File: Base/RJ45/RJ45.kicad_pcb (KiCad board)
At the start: 2 copper layers, 30 x 84 mm, 31 parts, among them J1 Barrel_Jack_Switch, J2 AudioJack2_Ground, J3 AudioJack2_Ground, J4 RJ45, U2 OPA1656

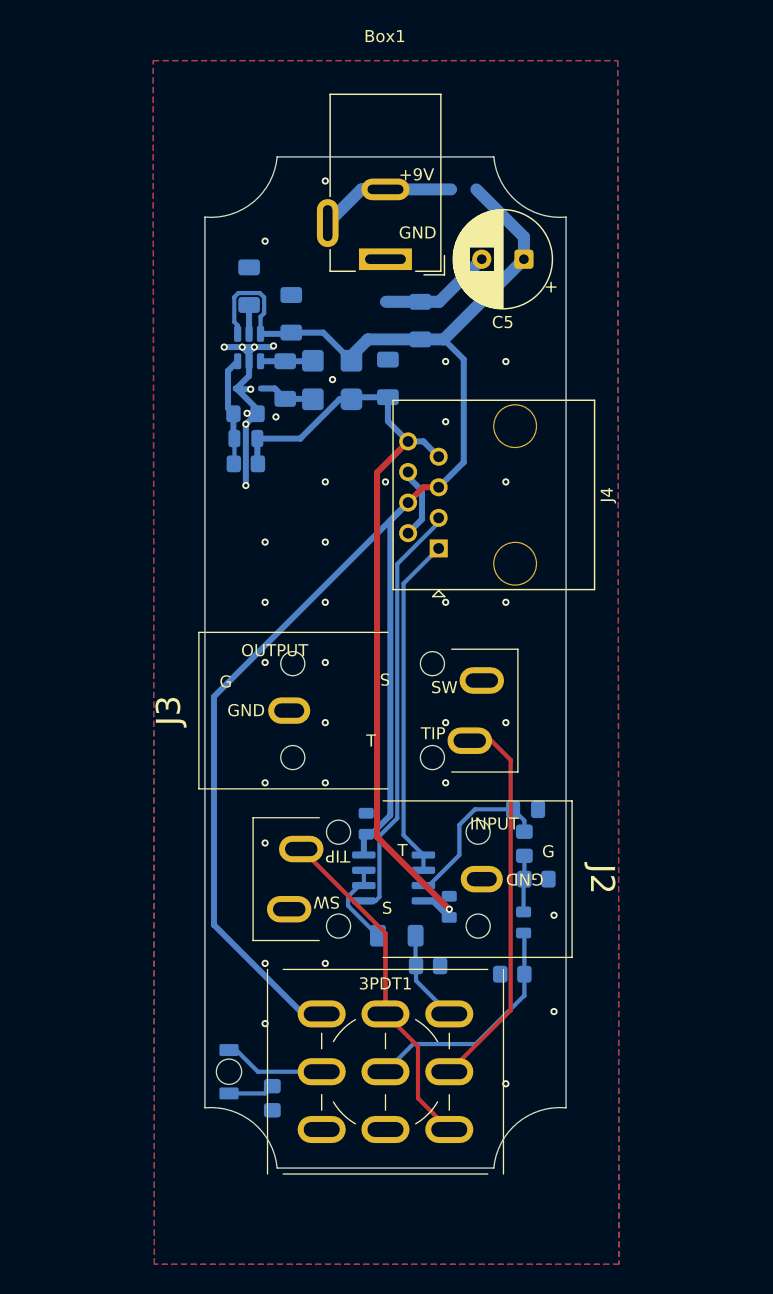
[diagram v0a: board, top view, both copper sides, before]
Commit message: Switch to a shielded RJ45 connector for the RJ45 test boards
It turns out that all my ethernet cables I had around look to be plain
unshielded twisted pairs (UTP), and some very preliminary testing shows
that they are very noisy and I'd need to use differential signalling to
make the whole "connect the base and effect with an ethernet cable"
scheme work.

I know, I know, that's technically the right thing to do anyway, but I
really don't think it's an option.  It adds way too much effort at the
effects end, at that point I'm better off just keeping the two together.

Even if some of my recent circuits have been differential (ie that whole
multiplier thing), I don't want to force that on everything.

And yes, the ethernet cable idea might have been a stupid idea and any
first-year EE would probably have told me that.  I'm a SW guy, remember?

But before giving up, let's just try the single-ended model with proper
shielded cables and shielded connectors.  The double-shielded cables are
a thing, with each twisted pair foil-shielded and then the whole cable
having a braided shield.

That would seem to be no worse than a normal 1/4" audio cable, even if
the same cable also carries power.  I'm looking for a few feet, not long
runs.  Knock wood.

And the shielding is part of the CAT8 specs, so this is standard cable
these days and cheap, even if my random box of cables was full of the
old crappy stuff of yesteryear.

So maybe this model is still salvageable with single-ended signaling.
Because I'd love to separate the stomp switch and audio jacks from the
actual effect side.

Signed-off-by: Linus Torvalds <torvalds@linux-foundation.org>
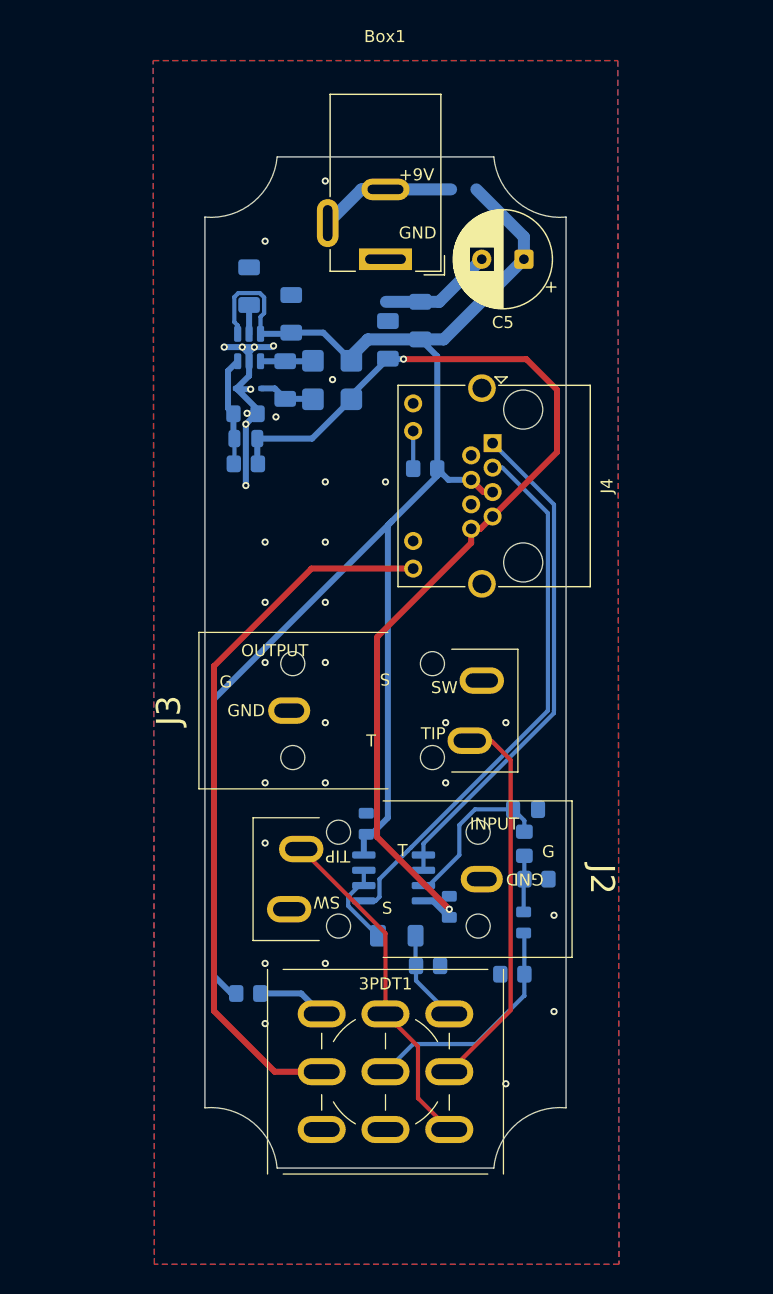
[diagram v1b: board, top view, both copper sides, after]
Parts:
- removed D3: LED, Mylib:Würth Reverse Mount LED
- added R1: 2.2k, Resistor_SMD:R_0805_2012Metric_Pad1.20x1.40mm_HandSolder, B.Cu at (103.3, 83.9)
- J4: value RJ45 -> RJ45_LED_Shielded; footprint Connector_RJ:RJ45_OST_PJ012-8P8CX_Vertical -> Connector_RJ:RJ45_Amphenol_RJHSE538X
- moved J4 9.83 mm to (108.9, 81.8), turned to -90 degrees
- moved R4 8.93 mm to (88.6, 127.5), turned to 0 degrees
- moved C4 3.20 mm to (100.2, 73.2)
- renumbered R1 to R2, R2 to R3, R3 to R4, R4 to R5, R5 to R6, R6 to R7, R7 to R8
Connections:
- 3PDT1 pad 1: +V -> Net-(3PDT1A-A1)
- 3PDT1 pad 2: Net-(3PDT1A-A2) -> LED^{ACTIVE}
- R4 pad 1: Net-(D3-K) -> +V
- R4 pad 2: GND -> Net-(3PDT1A-A1)
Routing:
- net LED^{ACTIVE}: track 0.00 -> 59.6 mm
- net -V: track 67.4 -> 86.7 mm, vias 1 -> 2
- net IN^{EFF}: track 28.6 -> 42.1 mm
- net OUT^{EFF}: track 34.6 -> 45.3 mm
- net Net-(3PDT1A-A2): track 7.85 -> 0.00 mm
- net Net-(3PDT1A-A1): track 0.00 -> 5.80 mm
- net GND: track 35.5 -> 29.9 mm, vias 39 -> 33
- net Net-(D3-K): track 3.85 -> 0.00 mm
- net +V: track 144.5 -> 140.7 mm
- net LED^{POWER}: track 0.00 -> 3.13 mm
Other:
- board text removed: "REF OUT IN +LED"

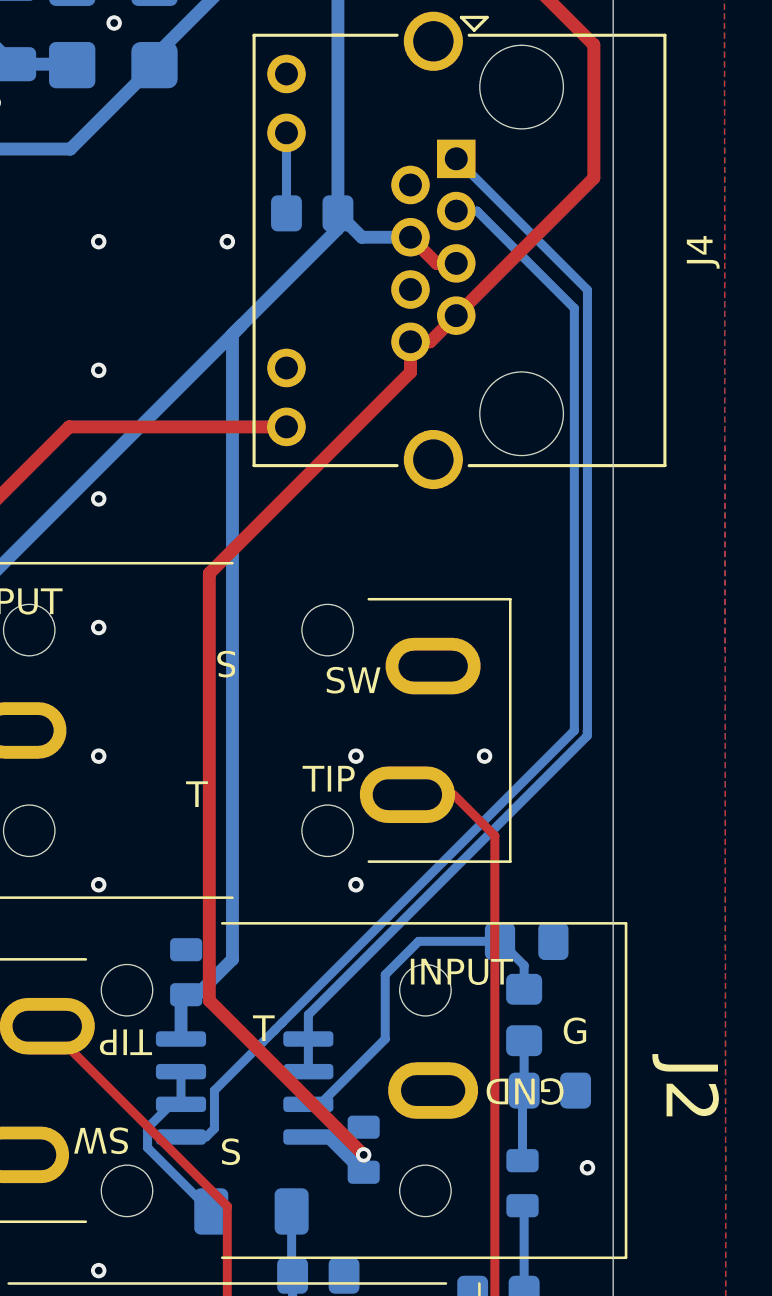
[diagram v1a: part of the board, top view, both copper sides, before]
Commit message: RJ45: hopefully make the base board actually work
Ok, with some boards back and populated, that whole "feed signal over
RJ45" didn't work at all.  I still think the concept should work, but my
implementation of it is obviously very broken.

The op amp output to the effect ends up oscillating wildly at a
frequency of a few MHz.  And while I might have screwed something else
up, I think it's because of a capacitive load in the form of that cable.

According to random searches I did, the minimal fix is typically to add
a small resistive load in series on the output.  So I did that.

But thinking about it, the other end is very possibly going to have the
same problem, and none of the existing effects boards were designed with
any of this in mind.

So I will also be updating the test board at the other end of the cable
to do active buffering and I suspect I really should rebias the signal
too at that point so that the existing effects boards see the
traditional VGND setup instead of the quick hack that just passively
changed the rules under them.

It may obviously still be the case that this is all just misguided
garbage, but before throwing it in the bin, let's try to do it right.
That includes adding some transmission line simulation, even if that
didn't actually show the issue (with or without the series resistor).

Maybe it's something else entirely that I'm not seeing / understanding.

Signed-off-by: Linus Torvalds <torvalds@linux-foundation.org>
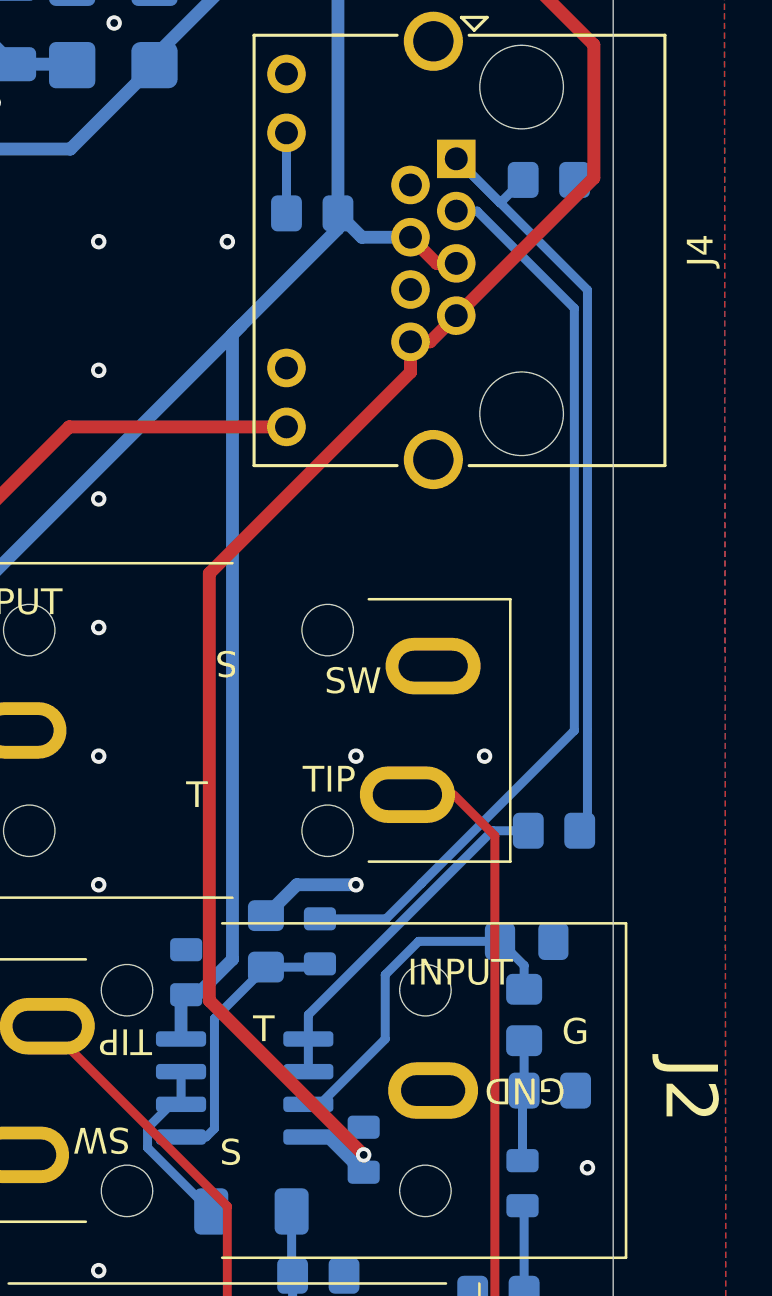
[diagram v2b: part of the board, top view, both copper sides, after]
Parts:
- added C12: 0.1uF, Mylib:C_0704_1810Metric, B.Cu at (103.6, 112.2)
- added R10: 100k, Resistor_SMD:R_0805_2012Metric_Pad1.20x1.40mm_HandSolder, B.Cu at (101.5, 112.2)
- added R6: 100R, Resistor_SMD:R_0805_2012Metric_Pad1.20x1.40mm_HandSolder, B.Cu at (112.7, 107.9)
- added R9: 100k, Resistor_SMD:R_0805_2012Metric_Pad1.20x1.40mm_HandSolder, B.Cu at (112.5, 82.6)
- renumbered C12 to C13, R8 to R11, R6 to R7, R7 to R8
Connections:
- U2 pad 1: IN^{EFF} -> Net-(U2A--)
- U2 pad 2: IN^{EFF} -> Net-(U2A--)
- U2 pad 5: OUT^{EFF} -> Net-(U2B-+)
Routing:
- net Net-(U2A--): track 0.00 -> 13.7 mm
- net Net-(U2B-+): track 0.00 -> 10.7 mm
- net IN^{EFF}: track 42.1 -> 32.0 mm
- net OUT^{EFF}: track 45.3 -> 35.5 mm
- net GND: track 29.9 -> 33.9 mm

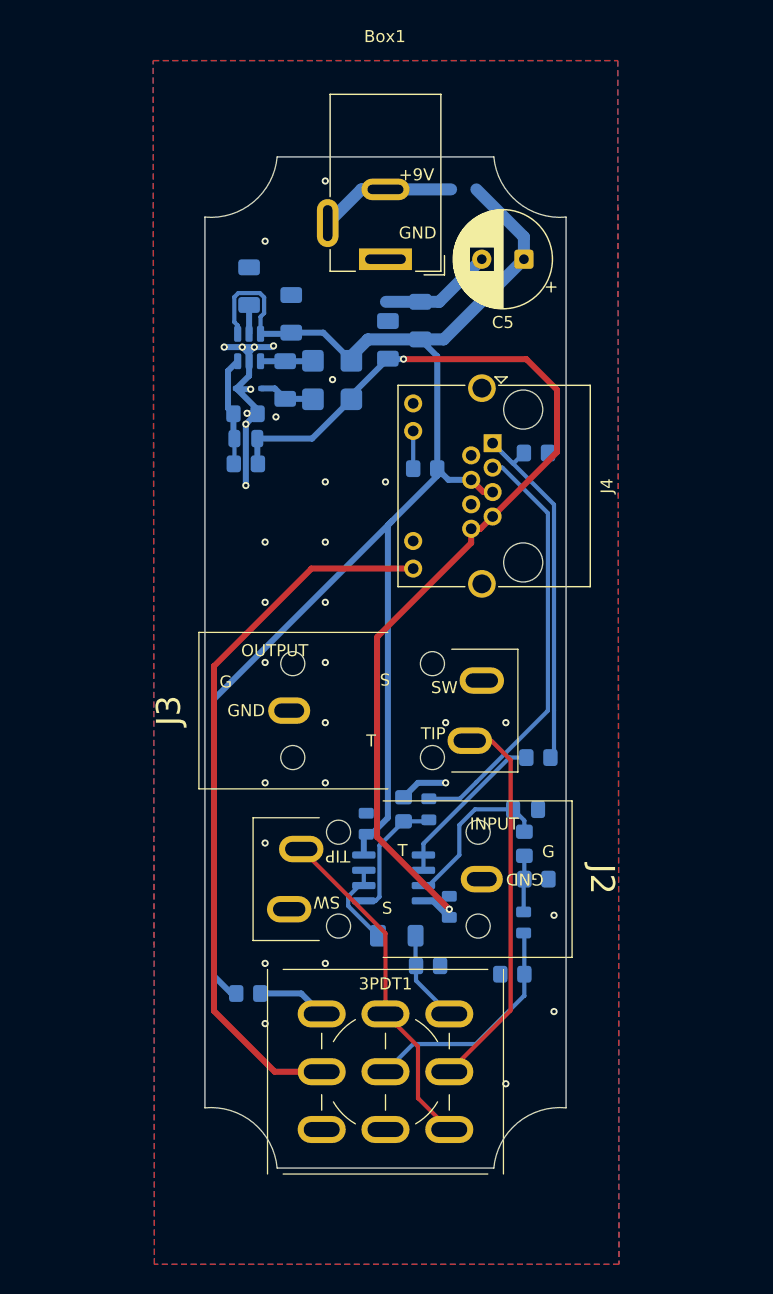
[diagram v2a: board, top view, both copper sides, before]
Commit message: Update the RJ45 boards
So I'm doing two different cable versions in parallel to see which I
like better.  The "passive base board" version uses USB-C connectors and
really doesn't do anything at all but convert the power, stomp switch
and audio connectors to one single cable.  So the effects board is
supposed to do everything that is actually signal-related, including
generating its own reference voltages etc.

In contrast, the RJ45 board is "active", and also generates a negative
power rail.  That doesn't help the existing effects boards, but it means
that any boards actively designed for this have all the voltages
(assuming +-9V and GND works for them), and don't need to rebias signals
etc.

Do I know which board - if any - I'm actually going to develop further?
No.  They may both be garbage.

Signed-off-by: Linus Torvalds <torvalds@linux-foundation.org>
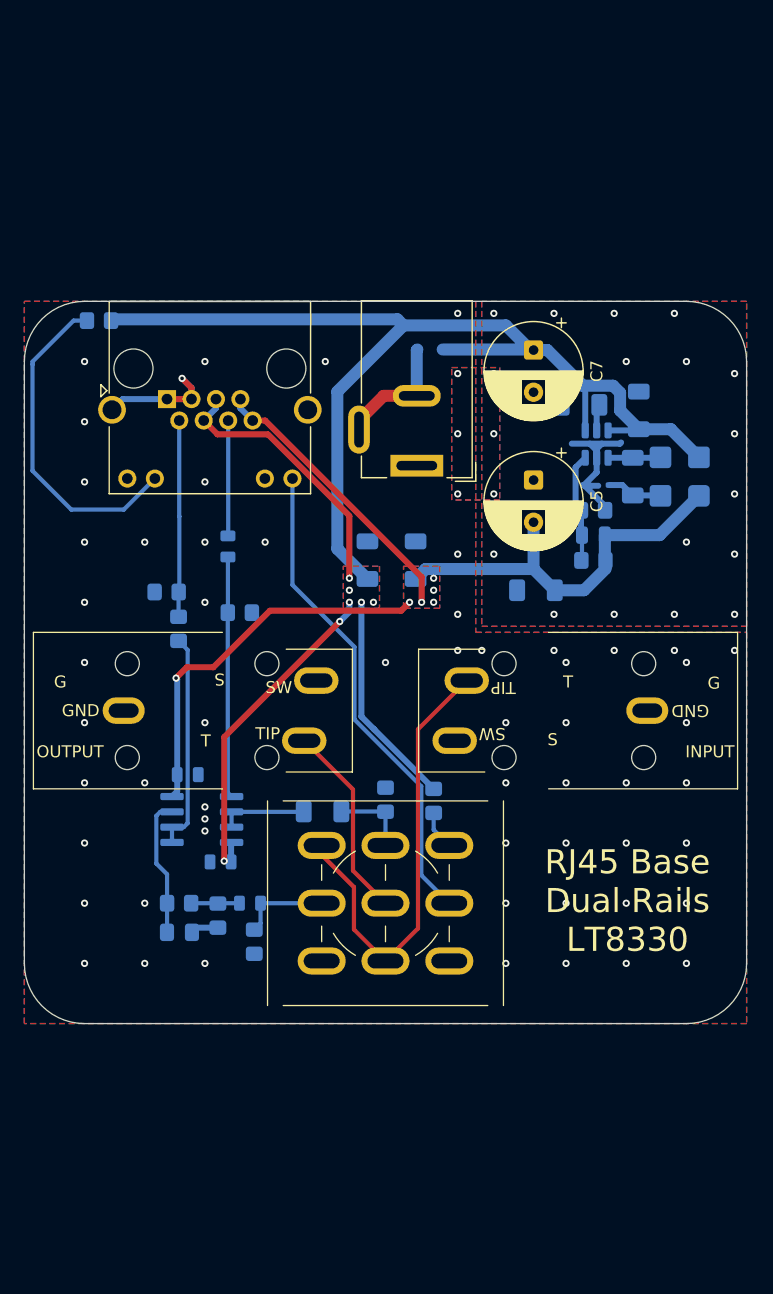
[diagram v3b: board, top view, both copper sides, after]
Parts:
- removed Box1: 1590A, Mylib:1590A
- added C5: 100uF, Capacitor_THT:CP_Radial_D8.0mm_P3.50mm, F.Cu at (112.3, 84.8)
- added C6: 10uF, Capacitor_SMD:C_1206_3216Metric_Pad1.33x1.80mm_HandSolder, B.Cu at (102.5, 91.5)
- moved R9 32.8 mm to (81.8, 94.1), turned to 180 degrees
- moved R6 31.7 mm to (82.8, 97.2), turned to 90 degrees
- moved C13 30.5 mm to (82.9, 122.4)
- moved C1 30.0 mm to (120.5, 84.6)
- moved C2 30.0 mm to (117.3, 89.4)
- moved C3 30.0 mm to (121.0, 79.1)
- moved D1 30.0 mm to (117.5, 85.3)
- moved L1 30.0 mm to (124.4, 84.6)
- moved R2 30.0 mm to (117.3, 91.5)
- moved R3 30.0 mm to (117.2, 87.4)
- moved U1 30.0 mm to (117.5, 81.9)
- moved R1 29.8 mm to (76.2, 71.6)
- moved C9 29.2 mm to (116.2, 78.6), turned to 180 degrees
- moved R5 29.1 mm to (82.9, 120.0), turned to 180 degrees
- moved C14 27.5 mm to (86.9, 90.4)
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- renumbered C8 to C10, C9 to C11, C10 to C12, C11 to C13, C12 to C14, C13 to C15, C5 to C7, C6 to C8, C7 to C9
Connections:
- 3PDT1 pad 1: Net-(3PDT1A-A1) -> IN^{CONN}
- 3PDT1 pad 2: LED^{ACTIVE} -> IN^{RAW}
- 3PDT1 pad 4: IN^{CONN} -> OUT^{RAW}
- 3PDT1 pad 5: IN^{RAW} -> OUT^{CONN}
- 3PDT1 pad 6: GND -> IN^{CONN}
- 3PDT1 pad 7: OUT^{RAW} -> Net-(3PDT1C-C1)
- 3PDT1 pad 8: OUT^{CONN} -> LED^{ACTIVE}
- 3PDT1 pad 9: IN^{CONN} -> GND
- J4 pad 1: IN^{EFF} -> GND
- J4 pad 2: GND -> IN^{EFF}
- J4 pad 3: OUT^{EFF} -> GND
- J4 pad 6: GND -> OUT^{EFF}
- R4 pad 2: Net-(3PDT1A-A1) -> Net-(3PDT1C-C1)
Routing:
- net OUT^{EFF}: track 35.5 -> 9.59 mm
- net LED^{POWER}: track 3.13 -> 27.6 mm
- net +V: track 140.7 -> 161.6 mm, vias 0 -> 7
- net LED^{ACTIVE}: track 59.6 -> 40.7 mm
- net IN^{EFF}: track 32.0 -> 16.5 mm
- net OUT^{CONN}: track 30.3 -> 16.3 mm
- net IN^{RAW}: track 19.3 -> 7.50 mm
- net IN^{CONN}: track 28.4 -> 37.9 mm
- net Net-(U2B-+): track 10.7 -> 20.0 mm
- net Net-(3PDT1A-A1): track 5.80 -> 0.00 mm
- net GND: track 33.9 -> 28.7 mm, vias 33 -> 80
- net Net-(U2A--): track 13.7 -> 18.2 mm
- net Net-(3PDT1C-C1): track 0.00 -> 3.27 mm
- net -V: track 86.7 -> 89.5 mm, vias 2 -> 6
- net Net-(U2A-+): track 13.3 -> 11.5 mm
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- added copper zone on B.Cu, net +V
- added copper zone on F.Cu, net +V
- added copper zone on B.Cu, net -V
- added copper zone on F.Cu, net -V
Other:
- board size 30 x 84 mm -> 60 x 60 mm
- board text added: "RJ45 Base Dual Rails LT8330"
- board text removed: "+9V GND"
